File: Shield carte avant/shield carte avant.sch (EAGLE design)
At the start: 22 parts, among them IC1 MCP2562-E_SN, IC2 MCP2515-I_SO, J1 22-05-7078-07, J2 22-05-7028-02, J3 22-05-7038-03, J5 22-05-7028-02, M1 ARDUINO_R3_ICSP

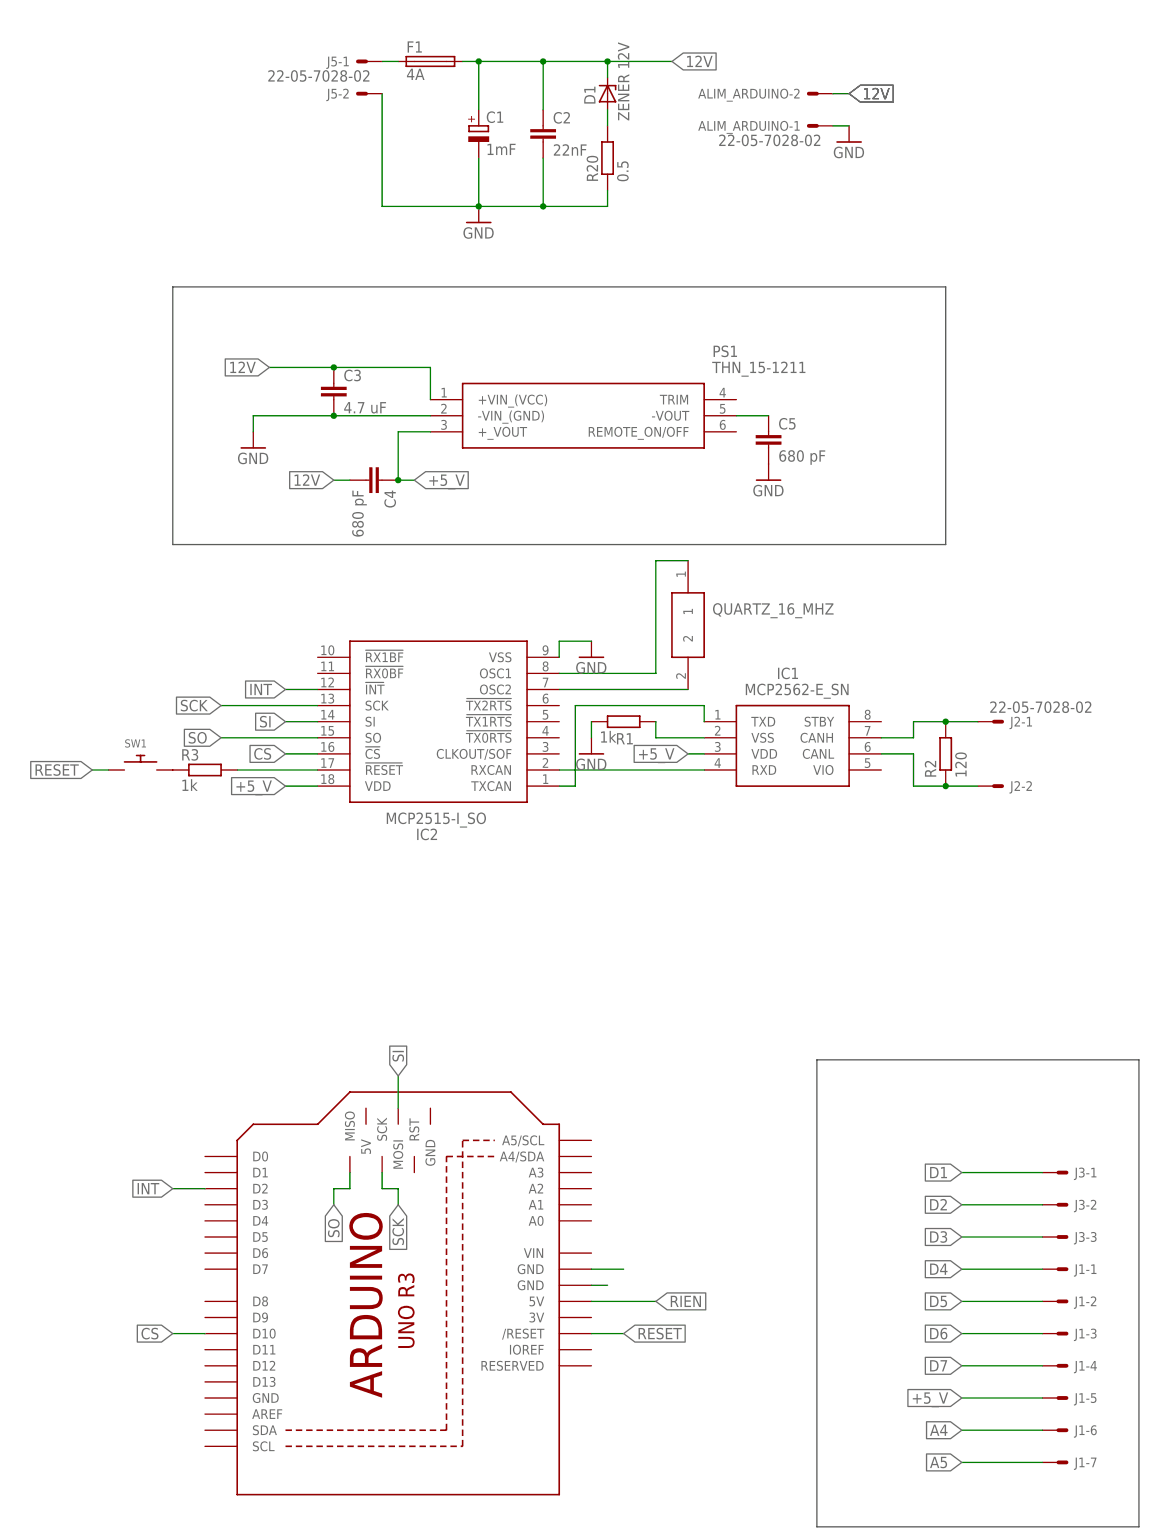
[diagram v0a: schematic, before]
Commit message: Alimentation de l'arduino par le 5V, passage des ic CAN en traversant et correction du schéma CAN
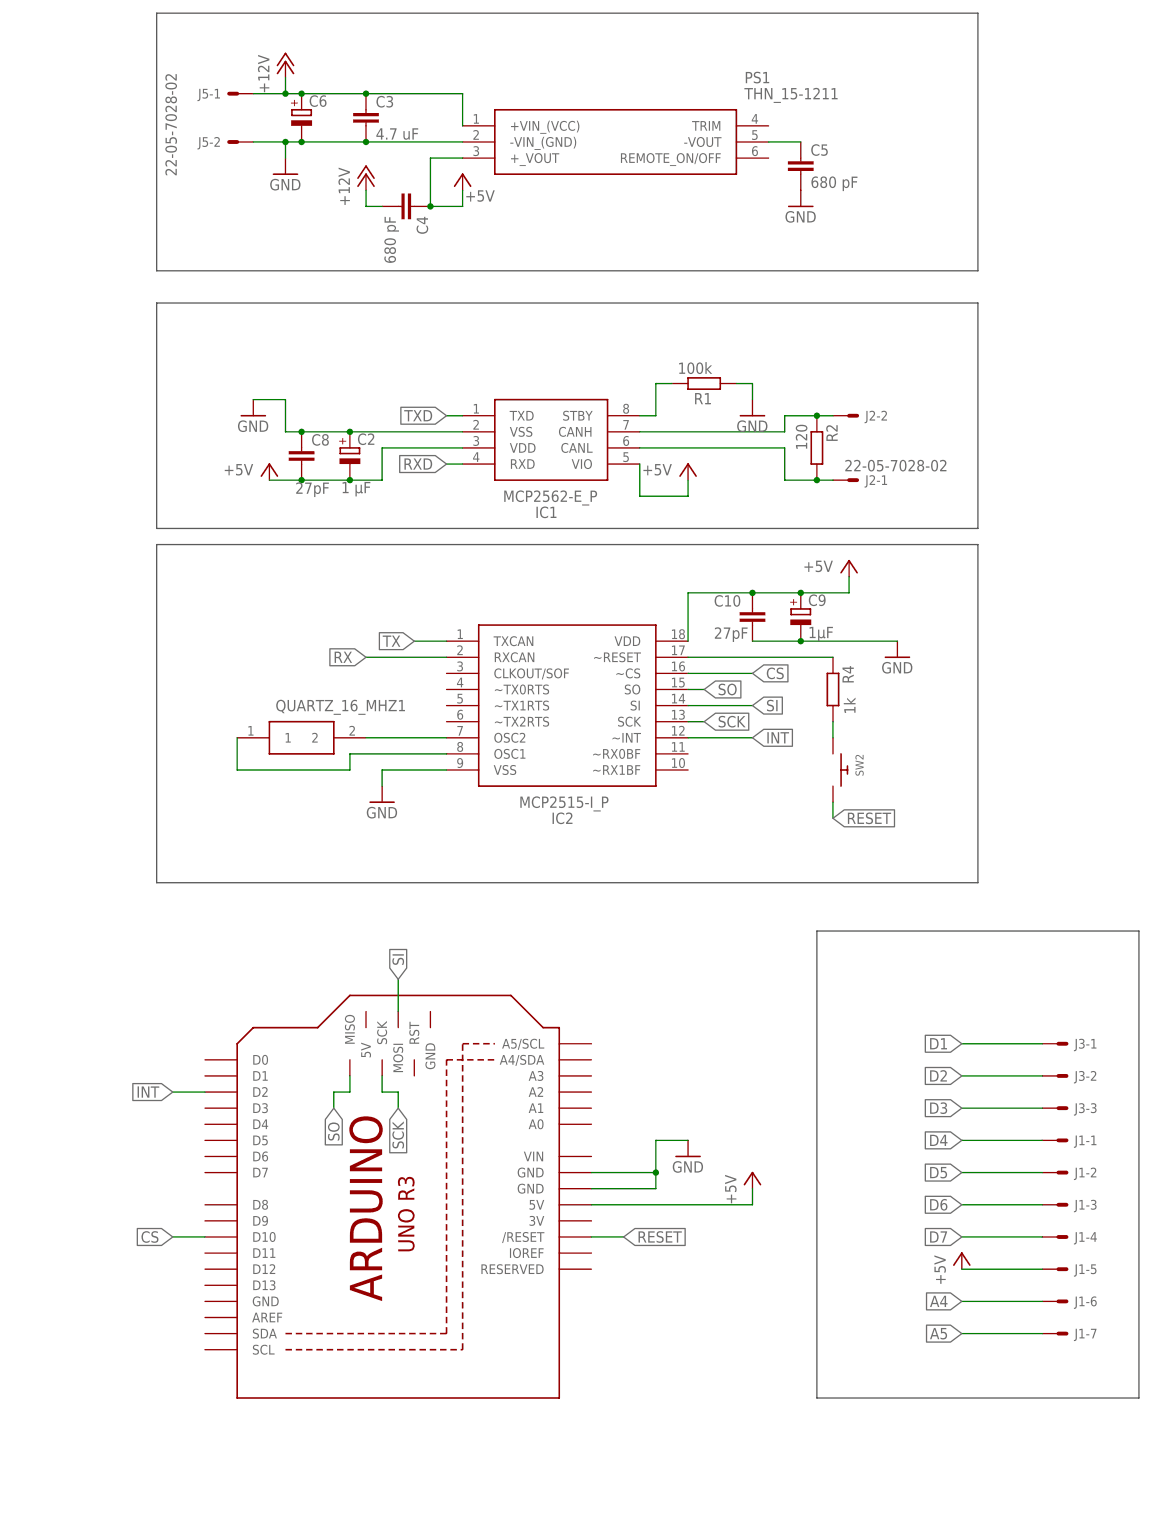
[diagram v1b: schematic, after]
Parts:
- removed ALIM_ARDUINO: 22-05-7028-02, EP_molex_6410_7395:22-05-7028-02
- removed C1: 1mF, rcl:CPOL-EUE7.5-16
- removed D1: ZENER 12V, diode:ZENER-DIODEDO41Z10
- removed F1: 4A, fuse:SH25
- removed QUARTZ_16_MHZ: FOXSLF_160-20, FOXSLF_160-20:FOXSLF_160-20
- removed R20: 0.5, resistor:R-EU_0309/12
- removed R3: 1k, rcl:R-EU_0204/7
- removed SW1: (no value), adafruit:SWITCH_PUSHBUTTONEVQ-PE
- added C10, C8: 27pF, rcl:C-EU025-030X050
- added C6: (no value), rcl:CPOL-EUB45181A
- added C9: 1µF, rcl:CPOL-EUB45181A
- added QUARTZ_16_MHZ1: FOXSLF_160-20, FOXSLF_160-20:FOXSLF_160-20
- added R4: 1k, rcl:R-EU_0204/7
- added SW2: (no value), adafruit:SWITCH_PUSHBUTTONEVQ-PE
- C2: value 22nF -> 1 µF; device rcl:C-EU025-025X050 -> rcl:CPOL-EUB45181A
- IC1: value MCP2562-E_SN -> MCP2562-E_P; device MCP2562-E_SN:MCP2562-E_SN -> MCP2562-E_P:MCP2562-E_P
- IC2: value MCP2515-I_SO -> MCP2515-I_P; device MCP2515-I_SO:MCP2515-I_SO -> MCP2515-I_P:MCP2515-I_P
- R1: value 1k -> 100k
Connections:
- removed net +5_V: C4.1, IC1.VDD, IC2.VDD, J1-5.S, PS1.+_VOUT
- removed net 12V: ALIM_ARDUINO-2.S, C1.+, C2.1, C3.1, C4.2, D1.C, F1.2, PS1.+VIN_(VCC)
- removed net N$10: IC2.OSC2, QUARTZ_16_MHZ.2
- removed net N$13: M1.GND@2
- removed net N$14: R3.1, SW1.P$2
- removed net N$15: IC2.!RESET, R3.2
- removed net N$16: M1.GND@1
- removed net N$9: IC1.CANL, J2-2.S, R2.1
- removed net RIEN: M1.5V
- new net +12V: C3.1, C4.2, C6.+, J5-1.S, PS1.+VIN_(VCC)
- new net +5V: C10.1, C2.-, C4.1, C8.2, C9.+, IC1.VDD, IC2.VDD, J1-5.S, M1.5V, PS1.+_VOUT
- new net N$2: R4.2, SW2.P$1
- new net RX: IC2.RXCAN
- new net RXD: IC1.RXD
- new net TX: IC2.TXCAN
- new net TXD: IC1.TXD
- net CS: now also IC2.~CS; no longer IC2.!CS
- net GND: now also C10.2, C2.+, C6.-, C8.1, C9.-, IC1.VSS, M1.GND@1, M1.GND@2; no longer ALIM_ARDUINO-1.S, C1.-, C2.2, R20.1
- net INT: now also IC2.~INT; no longer IC2.!INT
- net N$1: now also IC1.STBY, R1.2; no longer F1.1, J5-1.S
- net N$11: now also IC2.~RESET, R4.1; no longer IC2.OSC1, QUARTZ_16_MHZ.1
- net N$4: now also IC1.VIO; no longer D1.A, R20.2
- net N$5: now also IC1.CANH, J2-2.S, R2.1; no longer IC1.TXD, IC2.TXCAN
- net N$6: now also IC2.OSC2, QUARTZ_16_MHZ1.2; no longer IC1.RXD, IC2.RXCAN
- net N$7: now also IC2.OSC1, QUARTZ_16_MHZ1.1; no longer IC1.VSS, R1.2
- net N$8: now also IC1.CANL; no longer IC1.CANH
- net RESET: now also SW2.P$2; no longer SW1.P$1
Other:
- note added: "ALIMENTATION"
- note added: "CAN controller (copie du shield CANdiy)"
- note added: "CAN transceiver (copie du shield CANdiy)"
- note removed: "ALIMENTATION 12V"
- note removed: "ALIMENTATION 5V"
- moved on the sheet: C3, C4, C5, IC1, IC2, J1-1, J1-2, J1-3, J1-4, J1-5, J1-6, J1-7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

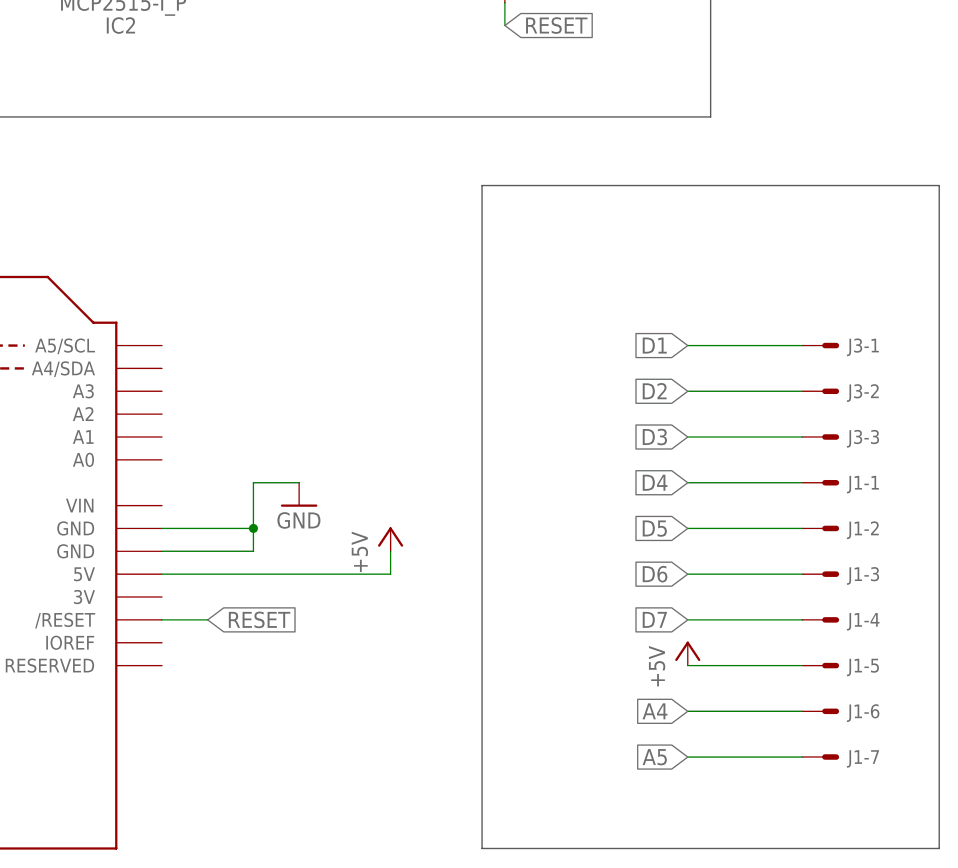
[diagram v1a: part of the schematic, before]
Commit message: Ajout des résistance de tirage de l'I2C
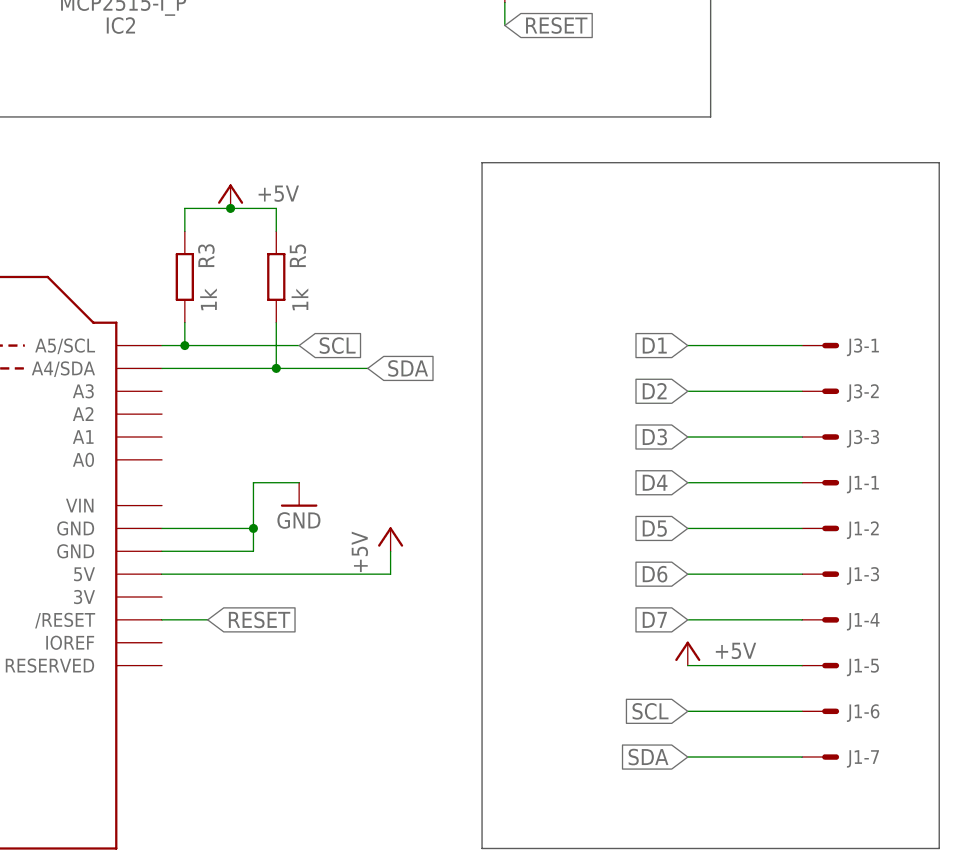
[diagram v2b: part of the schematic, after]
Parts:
- added R3, R5: 1k, rcl:R-EU_0204/7
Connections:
- removed net A4: J1-6.S
- removed net A5: J1-7.S
- new net SCL: J1-6.S, M1.A5/SCL, R3.2
- new net SDA: J1-7.S, M1.A4/SDA, R5.2
- net +5V: now also R3.1, R5.1
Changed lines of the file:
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@@
 <part name="GND1" library="supply1" deviceset="GND" device=""/>
 <part name="IC1" library="MCP2562-E_P" deviceset="MCP2562-E_P" device=""/>
+<part name="R3" library="rcl" library_urn="urn:adsk.eagle:library:334" deviceset="R-EU_" device="0204/7" package3d_urn="urn:adsk.eagle:package:23498/1" value="1k"/>
+<part name="R5" library="rcl" library_urn="urn:adsk.eagle:library:334" deviceset="R-EU_" device="0204/7" package3d_urn="urn:adsk.eagle:package:23498/1" value="1k"/>
+<part name="P+8" library="supply1" library_urn="urn:adsk.eagle:library:371" deviceset="+5V" device=""/>
 </parts>
 <sheets>
 <sheet>
 <plain>
-<wire x1="7.62" y1="106.68" x2="124.46" y2="106.68" width="0.1524" layer="249"/>
-<wire x1="124.46" y1="106.68" x2="124.46" y2="27.94" width="0.1524" layer="249"/>
+<wire x1="7.62" y1="109.22" x2="124.46" y2="109.22" width="0.1524" layer="249"/>
+<wire x1="124.46" y1="109.22" x2="124.46" y2="27.94" width="0.1524" layer="249"/>
 <wire x1="124.46" y1="27.94" x2="7.62" y2="27.94" width="0.1524" layer="249"/>
-<wire x1="7.62" y1="27.94" x2="7.62" y2="106.68" width="0.1524" layer="249"/>
-<text x="10.16" y="101.6" size="2.54" layer="249">Connection Pins Arduino</text>
+<wire x1="7.62" y1="27.94" x2="7.62" y2="109.22" width="0.1524" layer="249"/>
+<text x="10.16" y="104.14" size="2.54" layer="249">Connection Pins Arduino</text>
 <wire x1="22.86" y1="251.46" x2="152.4" y2="251.46" width="0.1524" layer="97"/>
 <wire x1="152.4" y1="251.46" x2="152.4" y2="210.82" width="0.1524" layer="97"/>
@@
 <wire x1="22.86" y1="210.82" x2="22.86" y2="251.46" width="0.1524" layer="97"/>
 <text x="78.74" y="246.38" size="2.54" layer="249">ALIMENTATION</text>
-<wire x1="127" y1="106.68" x2="177.8" y2="106.68" width="0.1524" layer="97"/>
-<wire x1="177.8" y1="106.68" x2="177.8" y2="33.02" width="0.1524" layer="97"/>
+<wire x1="127" y1="109.22" x2="177.8" y2="109.22" width="0.1524" layer="97"/>
+<wire x1="177.8" y1="109.22" x2="177.8" y2="33.02" width="0.1524" layer="97"/>
 <wire x1="177.8" y1="33.02" x2="127" y2="33.02" width="0.1524" layer="97"/>
-<wire x1="127" y1="33.02" x2="127" y2="106.68" width="0.1524" layer="97"/>
+<wire x1="127" y1="33.02" x2="127" y2="109.22" width="0.1524" layer="97"/>
 <text x="139.7" y="101.6" size="2.54" layer="249">Connection extérieur</text>
 <wire x1="22.86" y1="205.74" x2="152.4" y2="205.74" width="0.1524" layer="97"/>
@@
 </instance>
 <instance part="P+9" gate="1" x="149.86" y="55.88" smashed="yes">
-<attribute name="VALUE" x="147.32" y="50.8" size="1.778" layer="96" rot="R90"/>
+<attribute name="VALUE" x="157.48" y="55.88" size="1.778" layer="96" rot="R180"/>
 </instance>
 <instance part="GND8" gate="1" x="58.42" y="127" smashed="yes">
@@
 <attribute name="NAME" x="82.55" y="172.72" size="1.778" layer="95" align="center-left"/>
 <attribute name="VALUE" x="77.47" y="175.26" size="1.778" layer="96" align="center-left"/>
+</instance>
+<instance part="R3" gate="G$1" x="93.98" y="96.52" smashed="yes" rot="R270">
+<attribute name="NAME" x="95.4786" y="100.33" size="1.778" layer="95" rot="R270"/>
+<attribute name="VALUE" x="95.758" y="95.25" size="1.778" layer="96" rot="R270"/>
+</instance>
+<instance part="R5" gate="G$1" x="104.14" y="96.52" smashed="yes" rot="R270">
+<attribute name="NAME" x="105.6386" y="100.33" size="1.778" layer="95" rot="R270"/>
+<attribute name="VALUE" x="105.918" y="95.25" size="1.778" layer="96" rot="R270"/>
+</instance>
+<instance part="P+8" gate="1" x="99.06" y="106.68" smashed="yes">
+<attribute name="VALUE" x="106.68" y="106.68" size="1.778" layer="96" rot="R180"/>
 </instance>
 </instances>
@@
 </segment>
 </net>
-<net name="A4" class="0">
+<net name="SDA" class="0">
+<segment>
+<pinref part="M1" gate="G$1" pin="A4/SDA"/>
+<wire x1="91.44" y1="86.36" x2="104.14" y2="86.36" width="0.1524" layer="91"/>
+<label x="114.3" y="86.36" size="1.778" layer="95" xref="yes"/>
+<pinref part="R5" gate="G$1" pin="2"/>
+<wire x1="104.14" y1="86.36" x2="114.3" y2="86.36" width="0.1524" layer="91"/>
+<wire x1="104.14" y1="91.44" x2="104.14" y2="86.36" width="0.1524" layer="91"/>
+<junction x="104.14" y="86.36"/>
+</segment>
+<segment>
+<wire x1="162.56" y1="43.18" x2="149.86" y2="43.18" width="0.1524" layer="91"/>
+<label x="149.86" y="43.18" size="1.778" layer="95" rot="R180" xref="yes"/>
+<pinref part="J1" gate="-7" pin="S"/>
+</segment>
+</net>
+<net name="SCL" class="0">
+<segment>
+<pinref part="M1" gate="G$1" pin="A5/SCL"/>
+<wire x1="91.44" y1="88.9" x2="93.98" y2="88.9" width="0.1524" layer="91"/>
+<label x="106.68" y="88.9" size="1.778" layer="95" xref="yes"/>
+<pinref part="R3" gate="G$1" pin="2"/>
+<wire x1="93.98" y1="88.9" x2="106.68" y2="88.9" width="0.1524" layer="91"/>
+<wire x1="93.98" y1="91.44" x2="93.98" y2="88.9" width="0.1524" layer="91"/>
+<junction x="93.98" y="88.9"/>
+</segment>
 <segment>
 <wire x1="162.56" y1="48.26" x2="149.86" y2="48.26" width="0.1524" layer="91"/>
 <label x="149.86" y="48.26" size="1.778" layer="95" rot="R180" xref="yes"/>
 <pinref part="J1" gate="-6" pin="S"/>
-</segment>
-</net>
-<net name="A5" class="0">
-<segment>
-<wire x1="162.56" y1="43.18" x2="149.86" y2="43.18" width="0.1524" layer="91"/>
-<label x="149.86" y="43.18" size="1.778" layer="95" rot="R180" xref="yes"/>
-<pinref part="J1" gate="-7" pin="S"/>
 </segment>
 </net>
@@
 <pinref part="P+9" gate="1" pin="+5V"/>
 </segment>
-</net>
+<segment>
+<pinref part="R3" gate="G$1" pin="1"/>
+<wire x1="93.98" y1="101.6" x2="93.98" y2="104.14" width="0.1524" layer="91"/>
+<pinref part="P+8" gate="1" pin="+5V"/>
+<wire x1="93.98" y1="104.14" x2="99.06" y2="104.14" width="0.1524" layer="91"/>
+<pinref part="R5" gate="G$1" pin="1"/>
+<wire x1="99.06" y1="104.14" x2="104.14" y2="104.14" width="0.1524" layer="91"/>
+<wire x1="104.14" y1="104.14" x2="104.14" y2="101.6" width="0.1524" layer="91"/>
+<junction x="99.06" y="104.14"/>
+</segment>
+</net>
